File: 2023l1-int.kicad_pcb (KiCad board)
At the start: 2 copper layers, 185 x 188.1 mm, 123 parts, among them IC1 STM32F103CBTx, IC2 SN74LVC2G04DBVTG4, IC3 SN74LVC2G04DBVTG4, J1 52610-1433, J2 XT30, J3 PGMR, J4 FL, J5 FR, J6 BL, J7 BR, J8 XT60, SW1 STM RST, SW2 L SW, SW3 M SW, SW4 SW_SPDT, U2 CD74HC4067SM, U4 CD74HC4067SM, U5 VNH5050A-E, U6 VNH5050A-E, U7 VNH5050A-E, U8 VNH5050A-E, Y1 8Mhz

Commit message: idl kicad
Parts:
- added C1: 10n, footprints:cap0603, F.Cu at (220.6, 47.4)
- added C10: 10u, footprints:cap0603, F.Cu at (220.6, 59.0)
- added C11: 1000u, footprints:CAPAE1030X1270N, F.Cu at (225.5, 69.7)
- added C2: 220u, footprints:EIA-7343-D, F.Cu at (238.0, 48.9)
- added C3: 10u, footprints:cap0603, F.Cu at (220.6, 50.3)
- added C7: 1500pF, footprints:cap0603, F.Cu at (220.6, 53.2)
- added C8: 10n, footprints:cap0603, F.Cu at (220.6, 56.1)
- added C9: 220u, footprints:EIA-7343-D, F.Cu at (238.0, 54.8)
- added D1: SS54, footprints:DIOM5025X220N, F.Cu at (238.1, 35.0)
- added D2: 1N5401, Diode_THT:D_DO-201AD_P15.24mm_Horizontal, F.Cu at (228.1, 29.5)
- added D4: SS54, footprints:DIOM5025X220N, F.Cu at (238.1, 39.2)
- added L1: 15u, footprints:L_Sunlord_SWPA8040S, F.Cu at (212.1, 50.7)
- added L2: 15u, footprints:L_Sunlord_SWPA8040S, F.Cu at (212.1, 60.2)
- added Q1: STP75NF75, footprints:TO255P1040X460X2890-3, F.Cu at (236.3, 67.0)
- added Q2: AO3400A, Package_TO_SOT_SMD:SOT-23, F.Cu at (244.5, 42.5)
- added R31: 10K, footprints:res0603, F.Cu at (225.5, 47.4)
- added R32: 10K, footprints:res0603, F.Cu at (225.5, 50.3)
- added R34: 5K9, footprints:res0603, F.Cu at (225.5, 53.2)
- added R35: 20, footprints:res0603, F.Cu at (225.5, 56.1)
- added R36: 1K, footprints:res0603, F.Cu at (225.5, 59.0)
- added R39: 10K, footprints:res0603, F.Cu at (225.5, 61.9)
- added R40: 3K24, footprints:res0603, F.Cu at (230.4, 47.4)
- added R46: 10K, footprints:res0603, F.Cu at (230.4, 50.3)
- added U1: TPS5430DDA, Package_SO:TI_SO-PowerPAD-8_ThermalVias, F.Cu at (230.0, 36.1)
- added U3: TPS5430DDA, Package_SO:TI_SO-PowerPAD-8_ThermalVias, F.Cu at (230.0, 42.7)
- moved SW4 119.1 mm to (105.7, 22.5), turned to 90 degrees
- moved SW2 118.4 mm to (121.7, 22.5), turned to -90 degrees
- moved J3 114.9 mm to (109.9, 25.0), turned to 90 degrees
- moved IC2 11.6 mm to (82.7, 106.0)
- moved IC3 9.71 mm to (144.7, 106.0)
- moved C20 4.00 mm to (78.7, 109.6)
- moved C6 4.00 mm to (148.7, 102.4)
- moved R37 4.00 mm to (148.7, 109.6)
- moved R38 4.00 mm to (139.4, 98.6)
- moved R42 4.00 mm to (78.7, 102.4)
- moved R43 4.00 mm to (88.0, 113.4)
- moved U2 4.00 mm to (141.7, 106.0)
- moved U4 4.00 mm to (85.7, 106.0)
- moved C5 0.40 mm to (113.0, 122.7)
- moved C4 0.40 mm to (117.1, 122.7)
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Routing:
- net VCC: track 429.3 -> 0.00 mm
- net Net-(U4-I0): track 73.1 -> 0.00 mm
- net Net-(U2-I1): track 66.5 -> 0.00 mm
- net Net-(U4-I14): track 66.5 -> 0.00 mm
- net Net-(U4-I1): track 66.5 -> 0.00 mm
- net Net-(U2-I14): track 66.5 -> 0.00 mm
- net Net-(U4-I13): track 57.3 -> 0.00 mm
- net Net-(U4-I2): track 57.3 -> 0.00 mm
- net Net-(U2-I2): track 57.3 -> 0.00 mm
- net Net-(U2-I13): track 57.3 -> 0.00 mm
- net Net-(U2-I3): track 50.5 -> 0.00 mm
- net Net-(U4-I12): track 50.5 -> 0.00 mm
- net Net-(U2-I12): track 50.5 -> 0.00 mm
- net Net-(U4-I3): track 50.5 -> 0.00 mm
- net Net-(U2-I4): track 45.4 -> 0.00 mm
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
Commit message: kill me
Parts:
- removed C1, C8: 10n, footprints:cap0603
- removed C10, C3: 10u, footprints:cap0603
- removed C2, C9: 220u, footprints:EIA-7343-D
- removed D1, D4: SS54, footprints:DIOM5025X220N
- removed L1, L2: 15u, footprints:L_Sunlord_SWPA8040S
- removed R32, R44, R46: 10K, footprints:res0603
- removed R34: 5K9, footprints:res0603
- removed R40: 3K24, footprints:res0603
- removed SW2: L SW, footprints:SS12D00G3
- removed SW3: M SW, Connector_PinHeader_2.54mm:PinHeader_1x03_P2.54mm_Vertical
- removed U1, U3: TPS5430DDA, Package_SO:TI_SO-PowerPAD-8_ThermalVias
- added Boost1: ~, footprints:Boost, F.Cu at (105.0, 76.0)
- moved Q2 135.8 mm to (113.7, 79.2), turned to -90 degrees
- moved D2 122.4 mm to (121.3, 89.4), turned to 180 degrees
- moved R35 121.4 mm to (107.3, 83.6), turned to 90 degrees
- moved Q1 121.2 mm to (116.2, 83.6), turned to 180 degrees
- moved R39 116.8 mm to (109.9, 78.0)
- moved R31 115.5 mm to (113.7, 76.2), turned to 180 degrees
- moved C11 115.4 mm to (113.7, 98.0), turned to 180 degrees
- moved C7 113.9 mm to (109.9, 80.0)
- moved R36 108.3 mm to (120.1, 83.6), turned to -90 degrees
- moved J8 5.68 mm to (38.7, 106.0)
- moved J1 1.32 mm to (180.0, 106.0)
- moved IC3 1.00 mm to (143.7, 106.0)
- moved IC2 1.00 mm to (83.7, 106.0)
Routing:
- removed copper zone on F.Cu, net Net-(J3-Pin_1)

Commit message: I HATE DOING L1
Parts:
- removed SW4: SW_SPDT, footprints:SS12D00G3
- added C1: 10n, footprints:cap0603, F.Cu at (234.2, 67.0)
- added C10: 10u, footprints:cap0603, F.Cu at (206.6, 50.1)
- added C2: 220u, footprints:EIA-7343-D, F.Cu at (227.4, 68.4)
- added C3: 10u, footprints:cap0603, F.Cu at (206.6, 44.3)
- added C8: 10n, footprints:cap0603, F.Cu at (206.6, 47.2)
- added C9: 220u, footprints:EIA-7343-D, F.Cu at (226.2, 48.8)
- added D1: SS54, footprints:DIOM5025X220N, F.Cu at (232.6, 55.6)
- added D4: SS54, footprints:DIOM5025X220N, F.Cu at (218.0, 76.6)
- added L1: 15u, footprints:L_Sunlord_SWPA8040S, F.Cu at (230.6, 61.6)
- added L2: 15u, footprints:L_Sunlord_SWPA8040S, F.Cu at (215.1, 54.2)
- added R32: 10K, footprints:res0603, F.Cu at (206.6, 53.0)
- added R34: 5K9, footprints:res0603, F.Cu at (206.6, 55.9)
- added R40: 3K24, footprints:res0603, F.Cu at (206.6, 58.8)
- added R44: 10K, footprints:res0603, F.Cu at (103.0, 23.4)
- added R46: 10K, footprints:res0603, F.Cu at (206.6, 64.6)
- added SW2: L SW, Connector_PinHeader_2.54mm:PinHeader_1x03_P2.54mm_Vertical, F.Cu at (122.0, 20.0)
- added SW3: M SW, Connector_PinHeader_2.54mm:PinHeader_1x03_P2.54mm_Vertical, F.Cu at (106.0, 25.1)
- added U1: TPS5430DDA, Package_SO:TI_SO-PowerPAD-8_ThermalVias, F.Cu at (239.0, 64.2)
- added U3: TPS5430DDA, Package_SO:TI_SO-PowerPAD-8_ThermalVias, F.Cu at (213.3, 68.8)
- moved J3 0.13 mm to (110.0, 25.0)
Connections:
- J3 pad 1: Net-(J3-Pin_1) -> +3V3

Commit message: left with boost
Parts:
- removed Boost1: ~, footprints:Boost
- removed C1, C8: 10n, footprints:cap0603
- removed C10, C3: 10u, footprints:cap0603
- removed C2, C9: 220u, footprints:EIA-7343-D
- removed C7: 1500pF, footprints:cap0603
- removed D1, D4: SS54, footprints:DIOM5025X220N
- removed D2: 1N5401, Diode_THT:D_DO-201AD_P15.24mm_Horizontal
- removed H1, H10, H11, H12, H13, H14, H15, H16, H17, H18, H19, H2, H20, H3, H4, H5, H6, H7, H8, H9: MountingHole_Pad, MountingHole:MountingHole_3.2mm_M3_Pad_Via
- removed IC2, IC3: SN74LVC2G04DBVTG4, footprints:SOT95P280X145-6N
- removed J2: XT30, footprints:AMASS_XT30-F
- removed L1, L2: 15u, footprints:L_Sunlord_SWPA8040S
- removed Q1: STP75NF75, footprints:TO255P1040X460X2890-3
- removed Q2: AO3400A, Package_TO_SOT_SMD:SOT-23
- removed R31, R32, R39, R46: 10K, footprints:res0603
- removed R34: 5K9, footprints:res0603
- removed R35: 20, footprints:res0603
- removed R36: 1K, footprints:res0603
- removed R40: 3K24, footprints:res0603
- J1: footprint footprints:0526101433 -> footprints:526101433
- U1, U3: value TPS5430DDA -> ~; footprint Package_SO:TI_SO-PowerPAD-8_ThermalVias -> footprints:buck
- moved U1 136.7 mm to (102.7, 74.0), turned to 0 degrees
- moved U3 88.7 mm to (124.7, 74.0)
- moved R43 36.6 mm to (123.5, 122.0), turned to 180 degrees
- moved R41 18.1 mm to (123.9, 119.2)
- moved R42 16.1 mm to (94.1, 97.6), turned to 180 degrees
- moved C15 16.0 mm to (120.1, 112.6), turned to 180 degrees
- moved C12 15.6 mm to (114.3, 95.6), turned to 180 degrees
- moved R37 13.1 mm to (136.1, 113.0)
- moved C6 10.8 mm to (137.9, 101.4)
- moved C13 10.7 mm to (114.3, 98.5)
- moved U2 10.0 mm to (131.7, 106.0)
- moved U4 10.00 mm to (95.7, 106.0)
- moved C20 10.00 mm to (88.3, 106.8), turned to 180 degrees
- moved R38 8.96 mm to (130.5, 97.8), turned to 180 degrees
- moved C19 6.89 mm to (77.5, 98.5)
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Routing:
- removed copper zone on B.Cu, net GND
- removed copper zone on F.Cu, net GND
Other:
- outline, holes or cut-outs redrawn

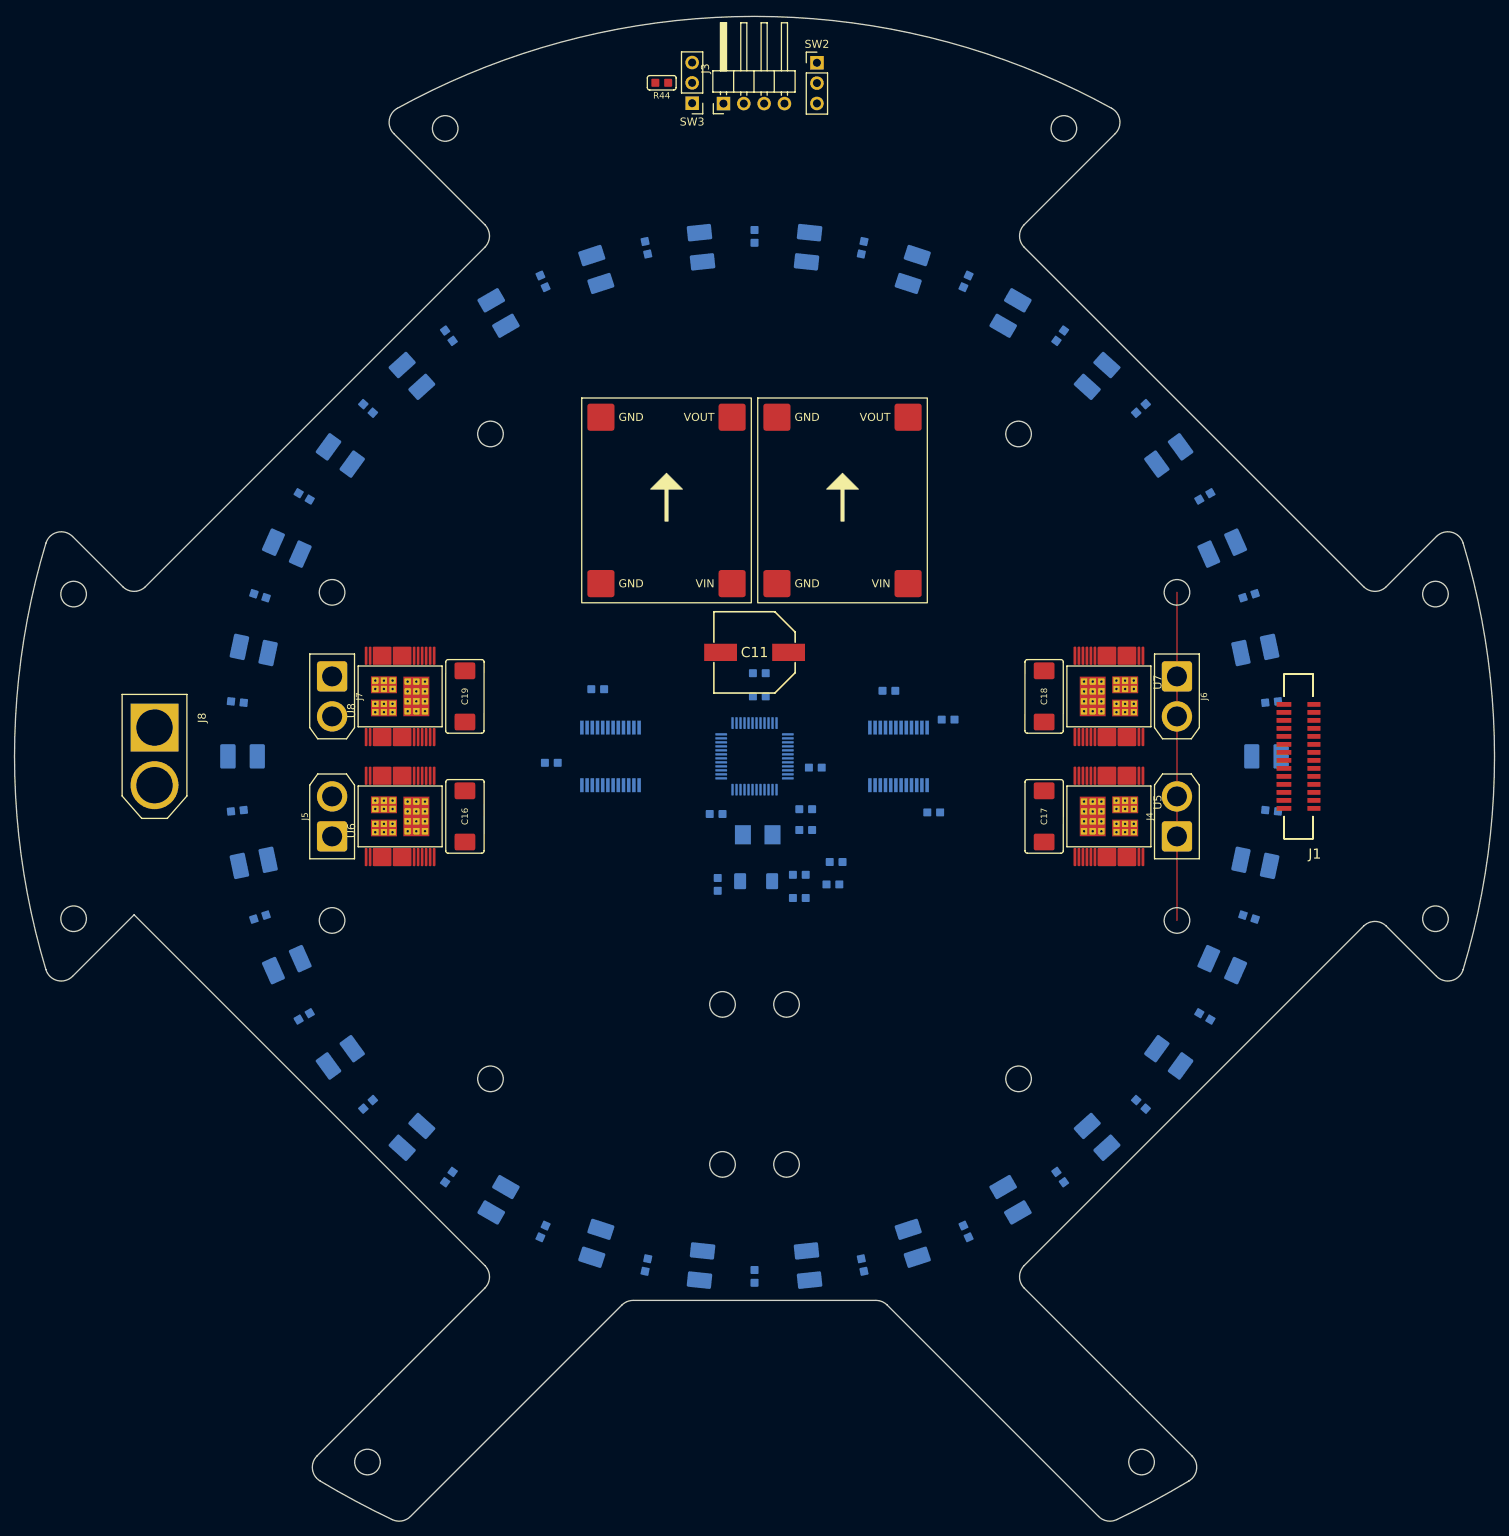
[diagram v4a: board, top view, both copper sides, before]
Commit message: done component placement
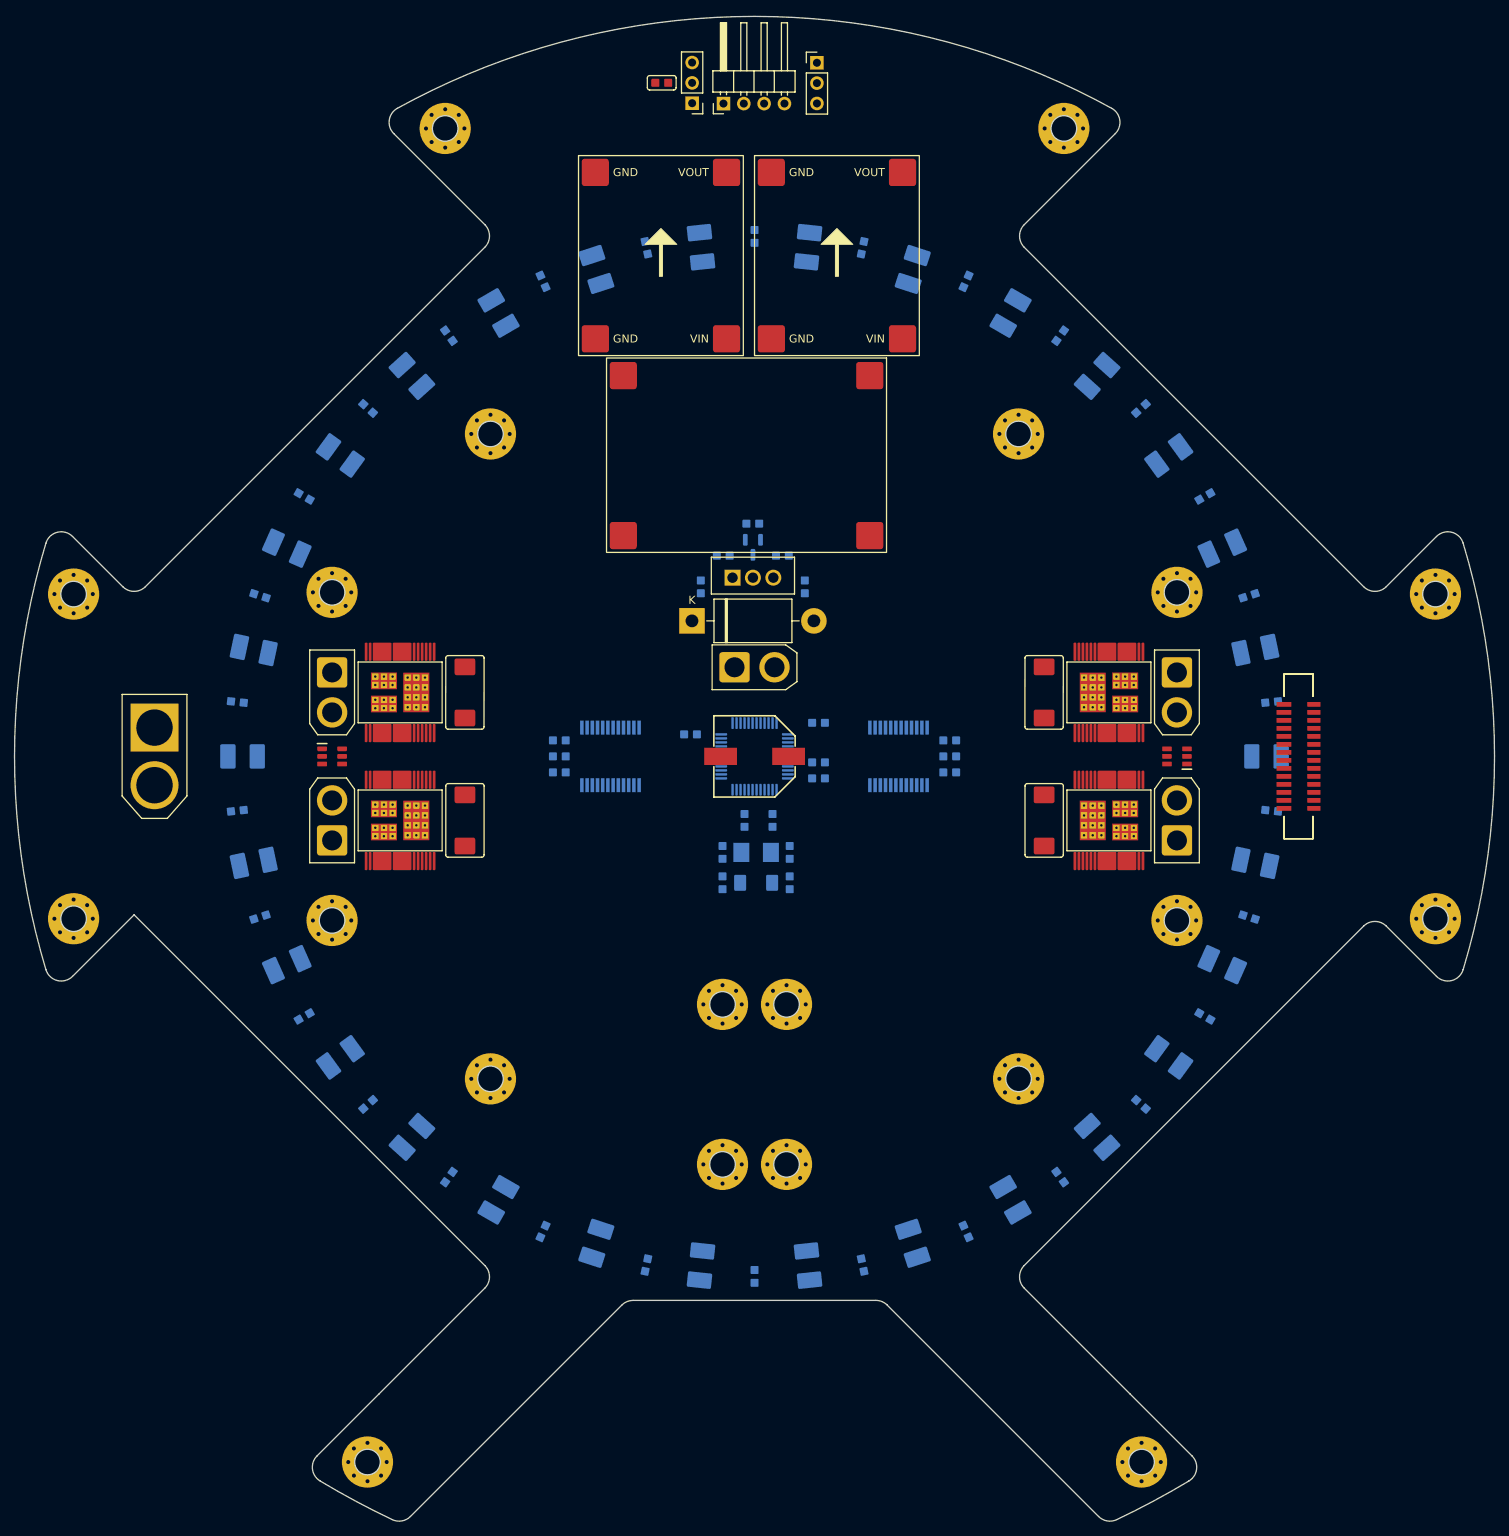
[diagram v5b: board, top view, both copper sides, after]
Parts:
- added Boost1: ~, footprints:boost, F.Cu at (112.7, 68.4)
- added C7: 1500pF, footprints:cap0603, B.Cu at (109.8, 80.9)
- added D2: 1N5401, Diode_THT:D_DO-201AD_P15.24mm_Horizontal, F.Cu at (105.9, 89.1)
- added H1: MountingHole_Pad, MountingHole:MountingHole_3.2mm_M3_Pad_Via, F.Cu at (65.3, 194.2)
- added H10: MountingHole_Pad, MountingHole:MountingHole_3.2mm_M3_Pad_Via, F.Cu at (166.5, 126.5)
- added H11: MountingHole_Pad, MountingHole:MountingHole_3.2mm_M3_Pad_Via, F.Cu at (28.6, 126.3)
- added H12: MountingHole_Pad, MountingHole:MountingHole_3.2mm_M3_Pad_Via, F.Cu at (198.8, 126.3)
- added H13: MountingHole_Pad, MountingHole:MountingHole_3.2mm_M3_Pad_Via, F.Cu at (28.6, 85.7)
- added H14: MountingHole_Pad, MountingHole:MountingHole_3.2mm_M3_Pad_Via, F.Cu at (60.9, 85.5)
- added H15: MountingHole_Pad, MountingHole:MountingHole_3.2mm_M3_Pad_Via, F.Cu at (166.5, 85.5)
- added H16: MountingHole_Pad, MountingHole:MountingHole_3.2mm_M3_Pad_Via, F.Cu at (198.8, 85.7)
- added H17: MountingHole_Pad, MountingHole:MountingHole_3.2mm_M3_Pad_Via, F.Cu at (80.7, 65.7)
- added H18: MountingHole_Pad, MountingHole:MountingHole_3.2mm_M3_Pad_Via, F.Cu at (146.7, 65.7)
- added H19: MountingHole_Pad, MountingHole:MountingHole_3.2mm_M3_Pad_Via, F.Cu at (75.0, 27.5)
- added H2: MountingHole_Pad, MountingHole:MountingHole_3.2mm_M3_Pad_Via, F.Cu at (162.1, 194.2)
- added H20: MountingHole_Pad, MountingHole:MountingHole_3.2mm_M3_Pad_Via, F.Cu at (152.3, 27.5)
- added H3: MountingHole_Pad, MountingHole:MountingHole_3.2mm_M3_Pad_Via, F.Cu at (109.7, 157.0)
- added H4: MountingHole_Pad, MountingHole:MountingHole_3.2mm_M3_Pad_Via, F.Cu at (117.7, 157.0)
- added H5: MountingHole_Pad, MountingHole:MountingHole_3.2mm_M3_Pad_Via, F.Cu at (80.7, 146.3)
- added H6: MountingHole_Pad, MountingHole:MountingHole_3.2mm_M3_Pad_Via, F.Cu at (146.7, 146.3)
- added H7: MountingHole_Pad, MountingHole:MountingHole_3.2mm_M3_Pad_Via, F.Cu at (109.7, 137.0)
- added H8: MountingHole_Pad, MountingHole:MountingHole_3.2mm_M3_Pad_Via, F.Cu at (117.7, 137.0)
- added H9: MountingHole_Pad, MountingHole:MountingHole_3.2mm_M3_Pad_Via, F.Cu at (60.9, 126.5)
- added IC2: SN74LVC2G04DBVTG4, footprints:SOT95P280X145-6N, F.Cu at (60.9, 106.0)
- added IC3: SN74LVC2G04DBVTG4, footprints:SOT95P280X145-6N, F.Cu at (166.5, 106.0)
- added J2: XT30, footprints:AMASS_XT30-F, F.Cu at (113.7, 94.9)
- added Q1: STP75NF75, footprints:TO255P1040X460X2890-3, F.Cu at (110.9, 83.7)
- added Q2: AO3400A, Package_TO_SOT_SMD:SOT-23, B.Cu at (113.5, 79.9)
- added R31: 10K, footprints:res0603, B.Cu at (113.5, 76.9)
- added R35: 20, footprints:res0603, B.Cu at (107.0, 84.8)
- added R36: 1K, footprints:res0603, B.Cu at (120.0, 84.8)
- added R39: 10K, footprints:res0603, B.Cu at (117.2, 80.9)
- moved R43 37.8 mm to (89.3, 106.0), turned to 0 degrees
- moved U1 30.6 mm to (102.0, 43.4)
- moved U3 30.6 mm to (124.0, 43.4)
- moved C11 13.0 mm to (113.7, 106.0)
- moved C12 11.5 mm to (105.7, 103.2)
- moved R38 11.2 mm to (138.1, 106.0)
- moved C5 11.2 mm to (109.7, 118.0), turned to -90 degrees
- moved C13 8.10 mm to (121.7, 101.8), turned to 0 degrees
- moved R42 8.00 mm to (89.3, 104.0), turned to 0 degrees
- moved R41 6.36 mm to (118.1, 121.8), turned to -90 degrees
- moved R37 5.39 mm to (138.1, 108.0)
- moved D3 4.32 mm to (115.9, 114.0), turned to 90 degrees
- moved C15 4.17 mm to (121.7, 108.7), turned to 0 degrees
- moved C14 3.64 mm to (112.4, 114.0), turned to -90 degrees
- moved C4 3.05 mm to (118.1, 118.0), turned to -90 degrees
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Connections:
- IC1 pad 12: unconnected-(IC1-PA2-Pad12) -> /SOL

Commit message: inital wiring
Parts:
- moved J1 2.00 mm to (183.7, 106.0)
- moved C20 1.60 mm to (89.3, 109.6)
- moved R42 1.60 mm to (89.3, 102.4)
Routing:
- net VCC: track 0.00 -> 423.0 mm
- net +5V: track 0.00 -> 103.8 mm, vias 0 -> 1
- net Net-(U4-I0): track 0.00 -> 67.4 mm
- net Net-(U2-I0): track 0.00 -> 67.4 mm
- net Net-(U4-I14): track 0.00 -> 60.7 mm
- net Net-(U4-I1): track 0.00 -> 60.7 mm
- net Net-(U4-I2): track 0.00 -> 58.5 mm
- net Net-(U4-I13): track 0.00 -> 58.5 mm
- net Net-(U4-I12): track 0.00 -> 56.4 mm
- net Net-(U4-I3): track 0.00 -> 56.4 mm
- net Net-(U4-I4): track 0.00 -> 51.3 mm
- net Net-(U4-I11): track 0.00 -> 51.3 mm
- net Net-(U4-I10): track 0.00 -> 51.0 mm
- net Net-(U4-I5): track 0.00 -> 51.0 mm
- net Net-(U4-I9): track 0.00 -> 48.3 mm
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- added copper zone on B.Cu, net GND
- added copper zone on F.Cu, net GND

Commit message: mux wiring done
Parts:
- moved R35 10.4 mm to (117.3, 86.0), turned to 180 degrees
- moved R36 10.4 mm to (109.7, 86.0), turned to 0 degrees
- moved R39 7.49 mm to (109.7, 80.8), turned to 0 degrees
- moved C7 6.30 mm to (113.5, 86.0), turned to 180 degrees
- moved R37 1.60 mm to (138.1, 109.6)
- moved C6 1.60 mm to (138.1, 102.4)
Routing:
- net Net-(U2-I14): track 0.00 -> 60.7 mm
- net Net-(U2-I1): track 0.00 -> 60.7 mm
- net Net-(U2-I13): track 0.00 -> 58.5 mm
- net Net-(U2-I2): track 0.00 -> 58.5 mm
- net Net-(U2-I3): track 0.00 -> 56.4 mm
- net Net-(U2-I12): track 0.00 -> 56.4 mm
- net Net-(U2-I11): track 0.00 -> 51.3 mm
- net Net-(U2-I4): track 0.00 -> 51.3 mm
- net Net-(U2-I5): track 0.00 -> 51.0 mm
- net Net-(U2-I10): track 0.00 -> 51.0 mm
- net Net-(U2-I6): track 0.00 -> 48.3 mm
- net Net-(U2-I9): track 0.00 -> 48.3 mm
- net Net-(U2-I8): track 0.00 -> 46.1 mm
- net Net-(U2-I7): track 0.00 -> 46.1 mm
- net +3V3: track 24.8 -> 36.3 mm
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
